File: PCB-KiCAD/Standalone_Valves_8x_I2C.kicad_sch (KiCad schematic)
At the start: 10 parts, among them J10 Conn_01x02, J11 Conn_01x02, J12 Conn_01x02, J13 Conn_01x02, J14 Conn_01x02, J7 Conn_01x02, J8 Conn_01x02, J9 Conn_01x02, U14 ULN2803A, U15 MCP23008-xP

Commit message: [PCB] More work on PCB v3
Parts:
- J10, J11, J12, J13, J14, J7, J8, J9: footprint (none) -> Connector_PinHeader_2.54mm:PinHeader_1x02_P2.54mm_Vertical
- U14: footprint (none) -> Package_DIP:DIP-18_W7.62mm
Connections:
- net +3.3V: no longer J10.2 (Pin_2), J11.2 (Pin_2), J12.2 (Pin_2), J13.2 (Pin_2), J14.2 (Pin_2), J7.2 (Pin_2), J8.2 (Pin_2), J9.2 (Pin_2)
- net at U14.1 (I1): now also U15.17 (GP7); no longer U15.10 (GP0)
- net at U14.2 (I2): now also U15.16 (GP6); no longer U15.11 (GP1)
- net at U14.3 (I3): now also U15.15 (GP5); no longer U15.12 (GP2)
- net at U14.4 (I4): now also U15.14 (GP4); no longer U15.13 (GP3)
- net at U14.5 (I5): now also U15.13 (GP3); no longer U15.14 (GP4)
- net at U14.6 (I6): now also U15.12 (GP2); no longer U15.15 (GP5)
- net at U14.7 (I7): now also U15.11 (GP1); no longer U15.16 (GP6)
- net at U14.8 (I8): now also U15.10 (GP0); no longer U15.17 (GP7)
- net A2: now reaches U15.3 (A2)
- net A1: now reaches U15.4 (A1)
- net A0: now reaches U15.5 (A0)
- new net +12V: J10.2 (Pin_2), J11.2 (Pin_2), J12.2 (Pin_2), J13.2 (Pin_2), J14.2 (Pin_2), J7.2 (Pin_2), J8.2 (Pin_2), J9.2 (Pin_2)
- no-connect marks 0 -> 2
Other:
- moved on the sheet: U15

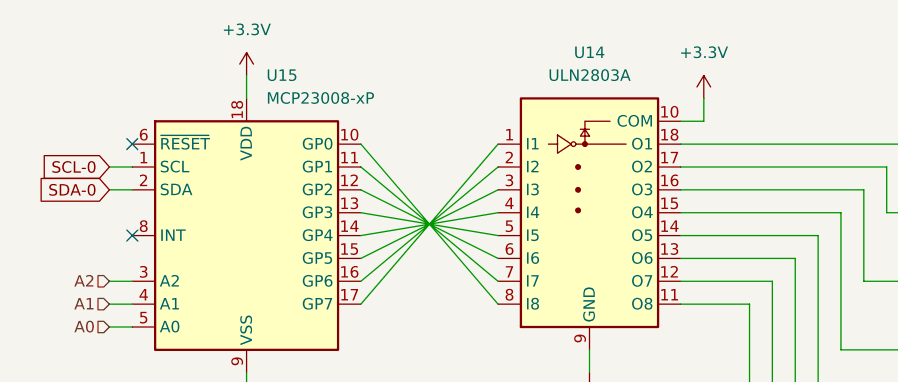
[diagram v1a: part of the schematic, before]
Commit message: Finalize PCB v3; Renumber to v4
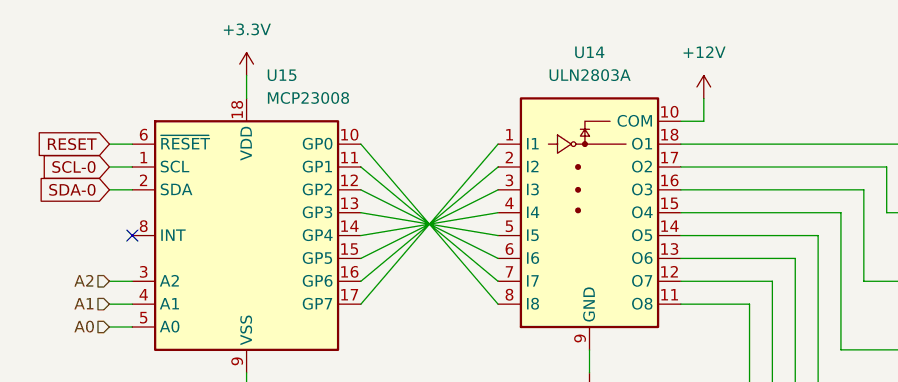
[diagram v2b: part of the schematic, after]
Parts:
- U15: value MCP23008-xP -> MCP23008
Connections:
- net +12V: now also U14.10 (COM)
- net +3.3V: no longer U14.10 (COM)
- net RESET: now reaches U15.6 (~{RESET})
- no-connect marks 2 -> 1
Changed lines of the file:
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@@
 		(at 40.64 50.8)
 	)
-	(no_connect
-		(at 40.64 40.64)
-	)
 	(wire
 		(pts
@@
 		(pts
 			(xy 116.84 71.12) (xy 116.84 50.8)
+		)
+		(stroke
+			(width 0)
+			(type default)
+		)
+	)
+	(wire
+		(pts
+			(xy 38.1 40.64) (xy 40.64 40.64)
 		)
 		(stroke
@@
 		(property "Intersheetrefs" "${INTERSHEET_REFS}"
 			(at 28.8253 43.18 0)
+			(effects
+				(font
+					(size 1.27 1.27)
+				)
+				(justify right)
+				(hide yes)
+			)
+		)
+	)
+	(global_label "RESET"
+		(shape input)
+		(at 38.1 40.64 180)
+		(fields_autoplaced yes)
+		(effects
+			(font
+				(size 1.27 1.27)
+			)
+			(justify right)
+		)
+		(property "Intersheetrefs" "${INTERSHEET_REFS}"
+			(at 29.3697 40.64 0)
 			(effects
 				(font
@@
 	)
 	(symbol
+		(lib_id "power:+12V")
+		(at 104.14 35.56 0)
+		(unit 1)
+		(exclude_from_sim no)
+		(in_bom yes)
+		(on_board yes)
+		(dnp no)
+		(fields_autoplaced yes)
+		(property "Reference" "#PWR03"
+			(at 104.14 39.37 0)
+			(effects
+				(font
+					(size 1.27 1.27)
+				)
+				(hide yes)
+			)
+		)
+		(property "Value" "+12V"
+			(at 104.14 30.48 0)
+			(effects
+				(font
+					(size 1.27 1.27)
+				)
+			)
+		)
+		(property "Footprint" ""
+			(at 104.14 35.56 0)
+			(effects
+				(font
+					(size 1.27 1.27)
+				)
+				(hide yes)
+			)
+		)
+		(property "Datasheet" ""
+			(at 104.14 35.56 0)
+			(effects
+				(font
+					(size 1.27 1.27)
+				)
+				(hide yes)
+			)
+		)
+		(property "Description" "Power symbol creates a global label with name \"+12V\""
+			(at 104.14 35.56 0)
+			(effects
+				(font
+					(size 1.27 1.27)
+				)
+				(hide yes)
+			)
+		)
+		(pin "1"
+		)
+		(instances
+			(project "HMS Olfactometer"
+				(path "/d7d8f86e-c8d6-438e-95be-a4e29dfe527f/189826bc-e86f-4673-87b3-0d281cb23bde"
+					(reference "#PWR03")
+					(unit 1)
+				)
+			)
+		)
+	)
+	(symbol
 		(lib_id "power:+3.3V")
 		(at 53.34 33.02 0)
@@
 				(path "/d7d8f86e-c8d6-438e-95be-a4e29dfe527f/189826bc-e86f-4673-87b3-0d281cb23bde"
 					(reference "#PWR01")
-					(unit 1)
-				)
-			)
-		)
-	)
-	(symbol
-		(lib_id "power:+3.3V")
-		(at 104.14 35.56 0)
-		(unit 1)
-		(exclude_from_sim no)
-		(in_bom yes)
-		(on_board yes)
-		(dnp no)
-		(fields_autoplaced yes)
-		(property "Reference" "#PWR03"
-			(at 104.14 39.37 0)
-			(effects
-				(font
-					(size 1.27 1.27)
-				)
-				(hide yes)
-			)
-		)
-		(property "Value" "+3.3V"
-			(at 104.14 30.48 0)
-			(effects
-				(font
-					(size 1.27 1.27)
-				)
-			)
-		)
-		(property "Footprint" ""
-			(at 104.14 35.56 0)
-			(effects
-				(font
-					(size 1.27 1.27)
-				)
-				(hide yes)
-			)
-		)
-		(property "Datasheet" ""
-			(at 104.14 35.56 0)
-			(effects
-				(font
-					(size 1.27 1.27)
-				)
-				(hide yes)
-			)
-		)
-		(property "Description" "Power symbol creates a global label with name \"+3.3V\""
-			(at 104.14 35.56 0)
-			(effects
-				(font
-					(size 1.27 1.27)
-				)
-				(hide yes)
-			)
-		)
-		(pin "1"
-		)
-		(instances
-			(project "HMS Olfactometer"
-				(path "/d7d8f86e-c8d6-438e-95be-a4e29dfe527f/189826bc-e86f-4673-87b3-0d281cb23bde"
-					(reference "#PWR03")
 					(unit 1)
 				)
@@
 			)
 		)
-		(property "Value" "MCP23008-xP"
+		(property "Value" "MCP23008"
 			(at 55.5341 35.56 0)
 			(effects
